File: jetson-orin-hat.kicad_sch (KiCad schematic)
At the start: 4 parts, among them J1 Conn_02x20_Counter_Clockwise, J2 I2C0, J3 I2C1, J4 UART

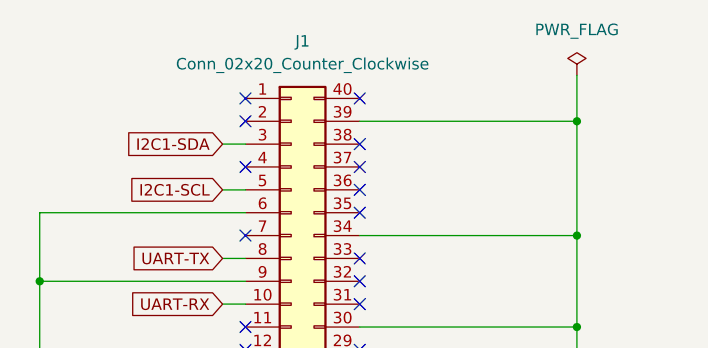
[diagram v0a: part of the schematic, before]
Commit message: done component placement
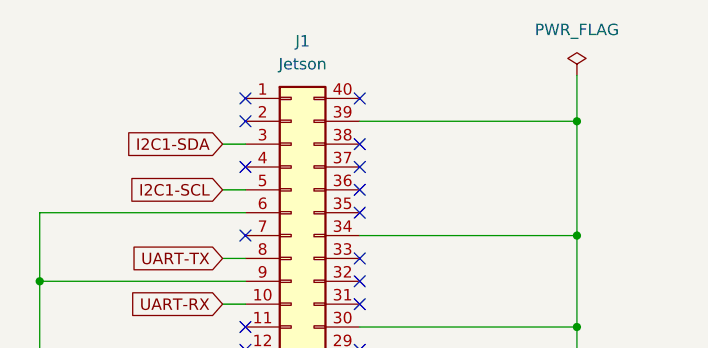
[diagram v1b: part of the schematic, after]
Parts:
- J1: value Conn_02x20_Counter_Clockwise -> Jetson
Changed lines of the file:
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@@
       (effects (font (size 1.27 1.27)))
     )
-    (property "Value" "Conn_02x20_Counter_Clockwise" (at 63.5 31.75 0)
+    (property "Value" "Jetson" (at 63.5 31.75 0)
       (effects (font (size 1.27 1.27)))
     )
